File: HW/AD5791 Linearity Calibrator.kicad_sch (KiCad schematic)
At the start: 62 parts, among them J10 Conn_01x01, J11 ISO OUT, J12 ISO OUT, J2 PWR, J3 REF, J4 REF, J5 REF, J6 REF, J7 Conn_01x01, J8 Conn_01x01, J9 Conn_01x01, SW1 RST, U1 Pico, U11 7533, U12 ADuM1201AR, U2 AD5791BRUZ, U3 LM399, U5 ADA4522-1, U6 ADA4522-1, U7 ADA4522-2, U8 78L15, U9 79L15

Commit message: updated files
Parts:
- U3: value LM399 -> ADR1399
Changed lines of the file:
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@@
   (symbol (lib_id "Reference_Voltage:LM399") (at 39.37 60.96 0) (unit 1)
     (in_bom yes) (on_board yes) (dnp no) (fields_autoplaced)
-    (property "Reference" "U3" (at 44.45 60.198 0)
+    (property "Reference" "U3" (at 44.45 59.563 0)
       (effects (font (size 1.27 1.27)) (justify left))
     )
-    (property "Value" "LM399" (at 44.45 62.738 0)
+    (property "Value" "ADR1399" (at 44.45 62.103 0)
       (effects (font (size 1.27 1.27)) (justify left))
     )

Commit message: rearranged files
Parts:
- removed C15, C17, C18, C9: 10uF, Resistor_SMD:R_0603_1608Metric, symbol Device:C_Small
- removed C5, C6, C7: 100uF, Capacitor_SMD:CP_Elec_6.3x5.4, symbol Device:C_Polarized_Small
- removed C8: 10nF, Resistor_SMD:R_0603_1608Metric, symbol Device:C_Small
- removed D1, D2, D4: 5819, Resistor_SMD:R_0603_1608Metric_Pad0.98x0.95mm_HandSolder, symbol Device:D_Small
- removed H1, H2, H3, H5: MountingHole_Pad, MountingHole:MountingHole_3.2mm_M3_Pad_Via, symbol Mechanical:MountingHole_Pad
- removed J10, J7, J8, J9: Conn_01x01, Connector_PinHeader_2.54mm:PinHeader_1x01_P2.54mm_Vertical, symbol Connector_Generic:Conn_01x01
- removed J11, J12: ISO OUT, Connector_PinHeader_2.54mm:PinHeader_1x04_P2.54mm_Vertical, symbol Connector_Generic:Conn_01x04
- removed J2: PWR, Connector_PinHeader_2.54mm:PinHeader_1x03_P2.54mm_Vertical, symbol Connector_Generic:Conn_01x03
- removed J4, J6: REF, Connector_PinHeader_2.54mm:PinHeader_1x02_P2.54mm_Vertical, symbol Connector_Generic:Conn_01x02
- removed JP1: GND BRIDGE, 0603 Jumper:0603 Jumper, symbol Jumper:SolderJumper_2_Open
- removed R1: R, Resistor_SMD:R_0603_1608Metric, symbol Device:R
- removed R10, R12, R13, R9: 10R, Resistor_SMD:R_0603_1608Metric, symbol Device:R
- removed R11: 10K, 0603 Jumper:0603 Jumper, symbol Device:R
- removed R14, R15, R4: 100K, Resistor_SMD:R_0603_1608Metric, symbol Device:R
- removed R2: 1K, Resistor_SMD:R_0603_1608Metric, symbol Device:R
- removed R3: 5R1, Resistor_SMD:R_0603_1608Metric, symbol Device:R
- removed U1: Pico, MCU_RaspberryPi_and_Boards:RPi_Pico_SMD_TH, symbol MCU_RaspberryPi_and_Boards:Pico
- removed U11: 7533, Package_TO_SOT_SMD:SOT-89-3, symbol Regulator_Linear:HT75xx-1-SOT89
- removed U12: ADuM1201AR, Package_SO:SOIC-8_3.9x4.9mm_P1.27mm, symbol Isolator:ADuM1201AR
- removed U5, U6: ADA4522-1, Package_SO:SOIC-8_3.9x4.9mm_P1.27mm, symbol Better Op-Amp:Better_Op-Amp
- removed U8: 78L15, Package_TO_SOT_SMD:SOT-89-3, symbol Regulator_Linear:L78L15_SOT89
- removed U9: 79L15, Package_TO_SOT_SMD:SOT-89-3, symbol Regulator_Linear:L79L15_SOT89
- added C1, C2, C3: 100uF, Capacitor_SMD:CP_Elec_6.3x5.4, symbol Device:C_Polarized_Small
- added C12, C9: 100nF, Capacitor_SMD:C_0603_1608Metric, symbol Device:C_Small
- added C9 (x2): 10uF, Resistor_SMD:R_0603_1608Metric, symbol Device:C_Small
- added J1, J4: ~, 100mm template footprints:CTB93HD3, symbol Connector_Generic:Conn_01x03
- added J11: SIG, Connector_PinHeader_1.27mm:PinHeader_1x04_P1.27mm_Vertical, symbol Connector_Generic:Conn_01x04
- added J11: PWR, Connector_PinHeader_2.54mm:PinHeader_1x04_P2.54mm_Vertical, symbol Connector_Generic:Conn_01x04
- added J2: VREFP, Connector_PinHeader_1.27mm:PinHeader_1x02_P1.27mm_Vertical, symbol Connector_Generic:Conn_01x02
- added J8: VREFN, Connector_PinHeader_1.27mm:PinHeader_1x02_P1.27mm_Vertical, symbol Connector_Generic:Conn_01x02
- added JP1: DACOUT, Connector_PinHeader_1.27mm:PinHeader_1x02_P1.27mm_Vertical, symbol Jumper:SolderJumper_2_Bridged
- added JP2: GND, Connector_PinHeader_1.27mm:PinHeader_1x02_P1.27mm_Vertical, symbol Jumper:SolderJumper_2_Bridged
- added R2: 1K, Resistor_SMD:R_0603_1608Metric, symbol Device:R
- added R2, R3, R4, R5: 10R, Resistor_SMD:R_0603_1608Metric, symbol Device:R
- added R3: 5R1, Resistor_SMD:R_0603_1608Metric, symbol Device:R
- added R4: 100K, Resistor_SMD:R_0603_1608Metric, symbol Device:R
- added U11: L79L15, Package_TO_SOT_SMD:SOT-89-3, symbol Regulator_Linear:L79L15_SOT89
- added U12: 7533, Package_TO_SOT_SMD:SOT-89-3, symbol Regulator_Linear:HT75xx-1-SOT89
- added U13: ADuM1400xRW, Package_SO:SOIC-16W_7.5x10.3mm_P1.27mm, symbol Isolator:ADuM1400xRW
- added U4: L78L15, Package_TO_SOT_SMD:SOT-89-3, symbol Regulator_Linear:L78L15_SOT89
- added U6: REFSCALE, Package_SO:SOIC-8_3.9x4.9mm_P1.27mm, symbol Device:Opamp_Dual
- added U8: Pico, MCU_RaspberryPi_and_Boards:RPi_Pico_SMD_TH, symbol MCU_RaspberryPi_and_Boards:Pico
- added U9: OUTBUF, Package_SO:SOIC-8_3.9x4.9mm_P1.27mm, symbol Device:Opamp_Dual
- C1, C16, C2, C3, C4: footprint Resistor_SMD:R_0603_1608Metric -> Capacitor_SMD:C_0603_1608Metric
- C10, C11, C13, C14: value 10uF -> 100nF; footprint Resistor_SMD:R_0603_1608Metric -> Capacitor_SMD:C_0603_1608Metric
- J3: value REF -> VREFN; footprint Connector_PinHeader_2.54mm:PinHeader_1x02_P2.54mm_Vertical -> Connector_PinHeader_1.27mm:PinHeader_1x02_P1.27mm_Vertical
- J5: value REF -> VREFP; footprint Connector_PinHeader_2.54mm:PinHeader_1x02_P2.54mm_Vertical -> Connector_PinHeader_1.27mm:PinHeader_1x02_P1.27mm_Vertical
- U7: value ADA4522-2 -> REFBUF
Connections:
- net FORCE+ is gone; now on net VREFNF: U7.1
- net FORCE- is gone; now on net VREFPF: U7.7
- net REF is gone; now on net 7VREF: U3.1
- net SENSE+ is gone; now on net VREFNS: U7.2 (-)
- net SENSE- is gone; now on net VREFPS: U7.6 (-)
- net ~{CLR} is gone; now on net +3.3V: U2.7 (~{CLR})
- net ~{RESET} is gone; now on net +3.3V: U2.6 (~{RESET})
- net +15V: now also C2.1, J11.4 (Pin_4), R2.1, R3.1, R4.1, R4.1, U12.2 (VIN), U4.1 (OUT); no longer J3.1 (Pin_1), R6.1, R7.1
- net +3.3V: now also C1.1, C9.2, J11.2 (Pin_2), U12.3 (VOUT), U13.16 (VDD2)
- net -15V: now also R6.1, R7.1, C3.2, J11.3 (Pin_3), R5.1, U11.3 (VO); no longer J5.1 (Pin_1)
- net 7VREF: now also J5.1 (Pin_1), R2.2, R3.1, R4.2, U6.5 (+)
- net ALERT: now also U8.21 (GPIO16)
- net GND: now also C2.2, U2.19 (AGND), U3.2, C1.2, C12.1, C2.2, C3.1, C9.1, C9.1, J1.2 (Pin_2), J11.1 (Pin_1), J2.2 (Pin_2), J4.2 (Pin_2), J8.1 (Pin_1), J8.2 (Pin_2), JP2.1 (A), JP2.2 (B), U11.1 (GND), U12.1 (GND), U13.15 (GND2), U13.9 (GND2), U4.2 (GND), U6.3 (+), U9.5 (+); no longer SW1.1 (A)
- net SCLK: now also U13.5 (VIC), U8.7 (GPIO5); no longer U2.13 (SCLK)
- net SDIN: now also U13.4 (VIB), U8.6 (GPIO4); no longer U2.12 (SDIN)
- net VREFNS: no longer RN1.14 (R3.2), RN1.15 (R2.2)
- net VREFPF: no longer D3.2 (A)
- net VREFPS: no longer RN1.10 (R7.2), RN1.9 (R8.2)
- net ~{LDAC}: now also U13.3 (VIA), U8.5 (GPIO3); no longer U2.8 (~{LDAC})
- net ~{SYNC}: now also U13.6 (VID), U8.9 (GPIO6); no longer U2.14 (~{SYNC})
- net at RN1.6 (R6.1): now also RN1.10 (R7.2); no longer RN1.1 (R1.1)
- net at R7.2: now also C14.2, U6.4 (V-); no longer C11.2
- net at RN1.12 (R5.2): now also RN1.11 (R6.2)
- net at RN1.5 (R5.1): now also RN1.4 (R4.1), U6.2 (-)
- net at SW1.2 (B): now also U8.30 (RUN)
- net at U7.8 (V+): now also C9.2, R2.2
- net at U7.4 (V-): now also C12.2, R5.2
- net at C2.1: now also R3.2
- net at RN1.2 (R2.1), RN1.3 (R3.1): now also U6.6 (-); no longer RN1.16 (R1.2)
- net +10.5V: now reaches D3.1 (K)
- net +10.5V: now also RN1.15 (R2.2), U7.5 (+), J2.1 (Pin_1), R2.1
- net at RN1.13 (R4.2): now also RN1.14 (R3.2)
- net at C13.2: now also R6.2, U9.4 (V-)
- net -10.5V: now reaches U7.3 (+)
- net -10.5V: now also J3.1 (Pin_1), RN1.7 (R7.1), U6.1
- net at C10.2: now also R3.2, U9.8 (V+); no longer R6.2
- net DACOUT renamed BUFIN
- net BUFIN: now also JP1.1 (A), JP1.2 (B), U9.3 (+)
- removed net GNDA: C2.2, U2.19 (AGND), U3.2, U7.5 (+)
- net SDO: no longer names the net of U2.11 (SDO)
- new net: J1.3 (Pin_3), U4.3 (IN)
- new net: J1.1 (Pin_1), U11.2 (VI)
- new net: J4.3 (Pin_3), U9.6 (-), U9.7
- new net: C11.2, R4.2, U6.8 (V+)
- new net: D3.2 (A), U6.7
- new net: J4.1 (Pin_1), U9.1, U9.2 (-)
- new net +3.3VP: C9.2, U13.1 (VDD1), U8.36 (3V3)
- new net GNDD: C9.1, SW1.1 (A), U13.2 (GND1), U13.8 (GND1), U8.13 (GND), U8.18 (GND), U8.23 (GND), U8.28 (GND), U8.3 (GND), U8.33 (AGND), U8.38 (GND), U8.42 (GND), U8.8 (GND)
- new net ISO SCLK: J11.3 (Pin_3), U13.12 (VOC), U2.13 (SCLK)
- new net ISO SDIN: J11.2 (Pin_2), U13.13 (VOB), U2.12 (SDIN)
- new net ISO ~{LDAC}: J11.1 (Pin_1), U13.14 (VOA), U2.8 (~{LDAC})
- new net ISO ~{SYNC}: J11.4 (Pin_4), U13.11 (VOD), U2.14 (~{SYNC})
- now unconnected: RN1.8 (R8.1)
- no-connect marks 10 -> 7
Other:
- note added: ">3mA Iz"
- note added: "cope cage 2333-MS544-10S-ND"
- note removed: "On-board 3V3 reg deactivated"
- note removed: "R should be calculated such that the impedance seen on both pins of the output stage op-amp are the same to prevent bias current errors. AD5791 nominal output imepdance is 3.4K, and assuming a 10K/10K divider with a 5K output impedance, R should be 1.6K. Not particularly important with modern op-amps."
- note removed: "SHORTED BY DEFAULT"
- note removed: "Select for 3mA Iz"

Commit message: further finishing touches
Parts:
- added J10, J11, J12, J13, J9: PWR, Connector_PinHeader_2.54mm:PinHeader_1x02_P2.54mm_Vertical, symbol Connector_Generic:Conn_01x02
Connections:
- net +15V: now also J9.1 (Pin_1)
- net +3.3V: now also J11.1 (Pin_1)
- net -15V: now also J10.1 (Pin_1)
- net GND: now also J10.2 (Pin_2), J11.2 (Pin_2), J12.2 (Pin_2), J13.2 (Pin_2), J9.2 (Pin_2)
- net VCC: now reaches J1.3 (Pin_3), U4.3 (IN)
- net VCC: now also J12.1 (Pin_1)
- net VSS: now reaches J1.1 (Pin_1), U11.2 (VI)
- net VSS: now also J13.1 (Pin_1)
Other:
- moved on the sheet: C1, C10, C11, C12, C13, C14, C2, C3, C9, J1, J11, J2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

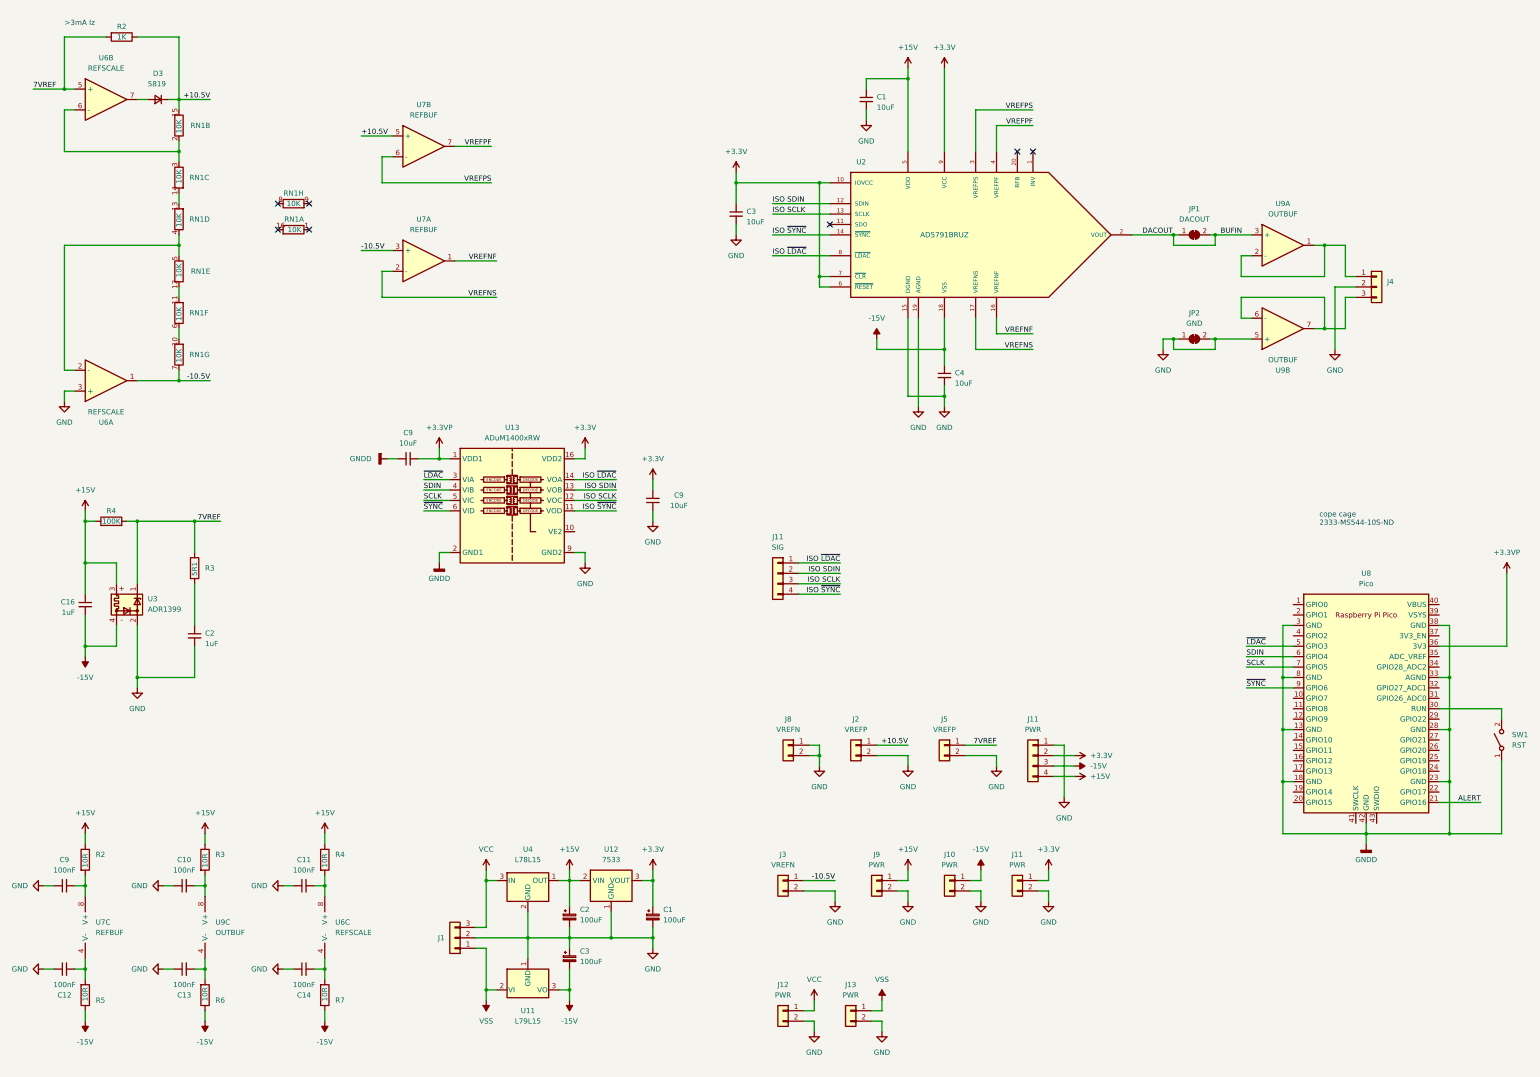
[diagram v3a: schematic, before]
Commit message: Update AD5791 Linearity Calibrator.kicad_sch
added annotations for specific parts choices (op-amps)
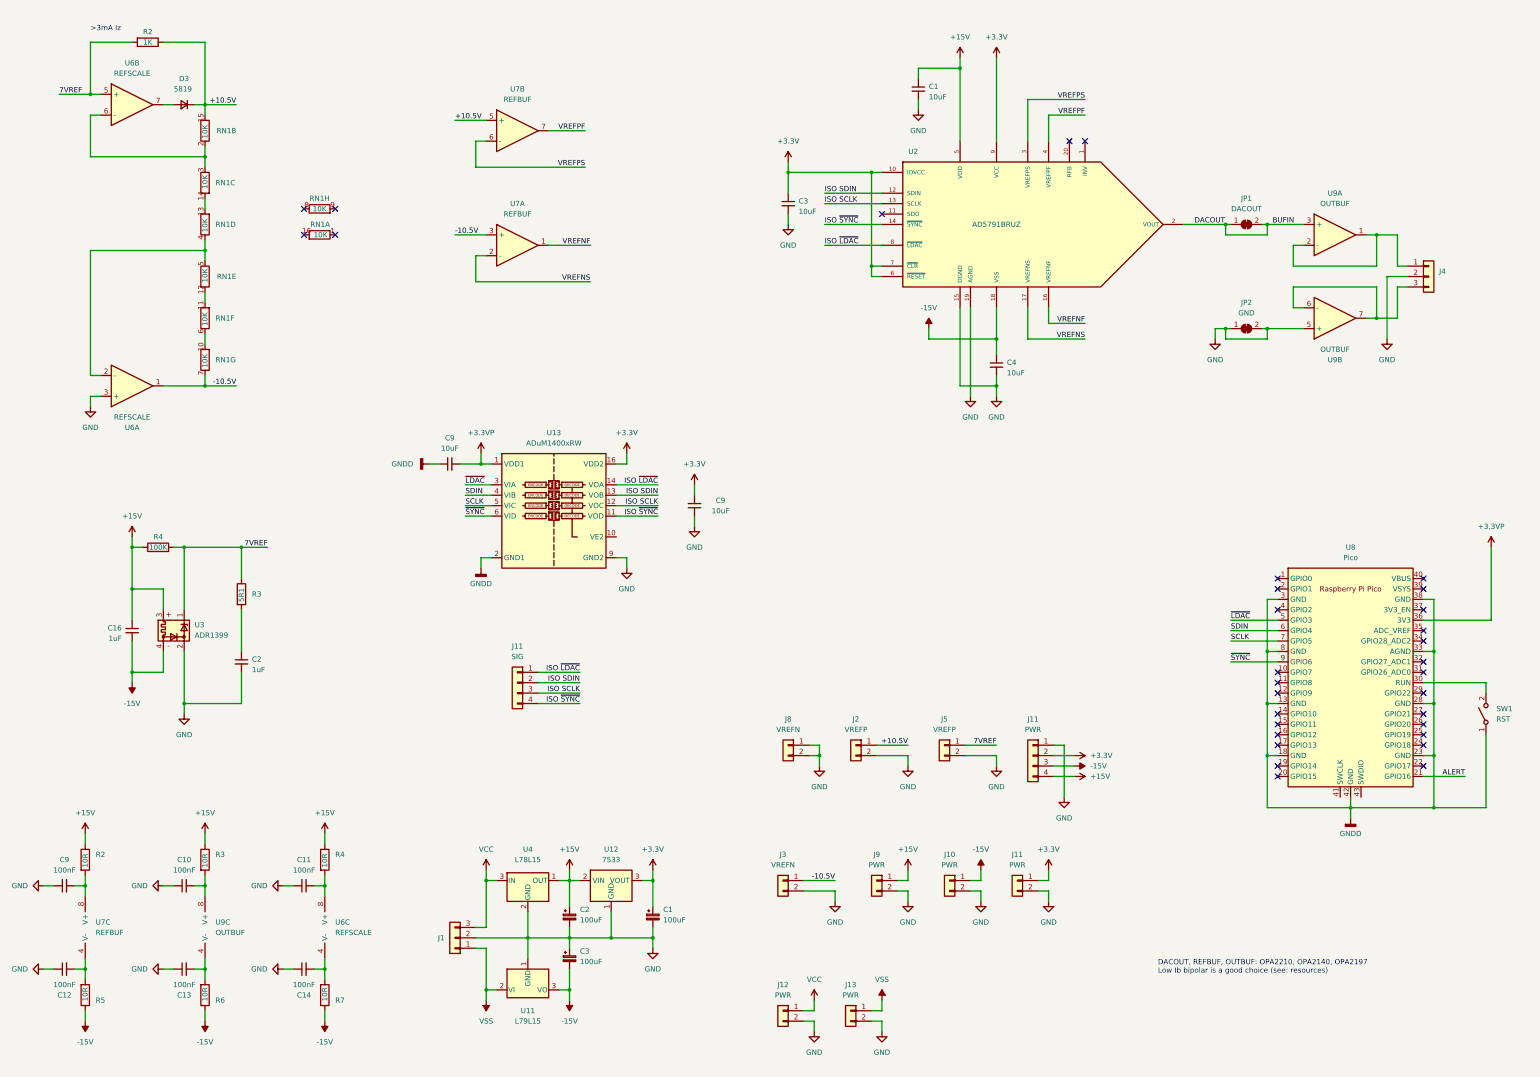
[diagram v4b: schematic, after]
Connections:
- no-connect marks 7 -> 32
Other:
- note added: "DACOUT, REFBUF, OUTBUF: OPA2210, OPA2140, OPA2197 Low Ib bipolar is a good choice (see: resources)"
- note removed: "cope cage 2333-MS544-10S-ND"
- moved on the sheet: C1, C16, C2, C3, C4, C9, D3, J11, J4, JP1, JP2, R2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

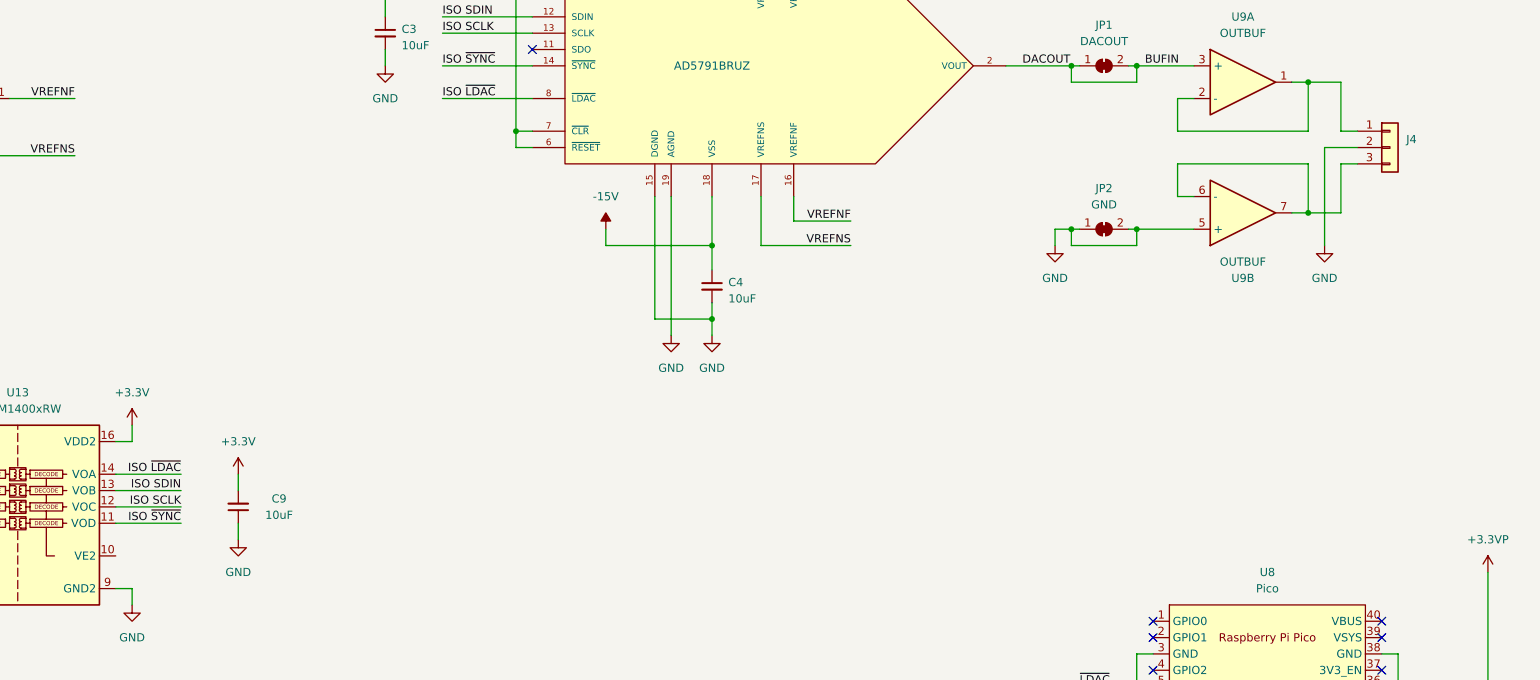
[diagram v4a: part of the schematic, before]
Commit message: added net and silkscreen labels
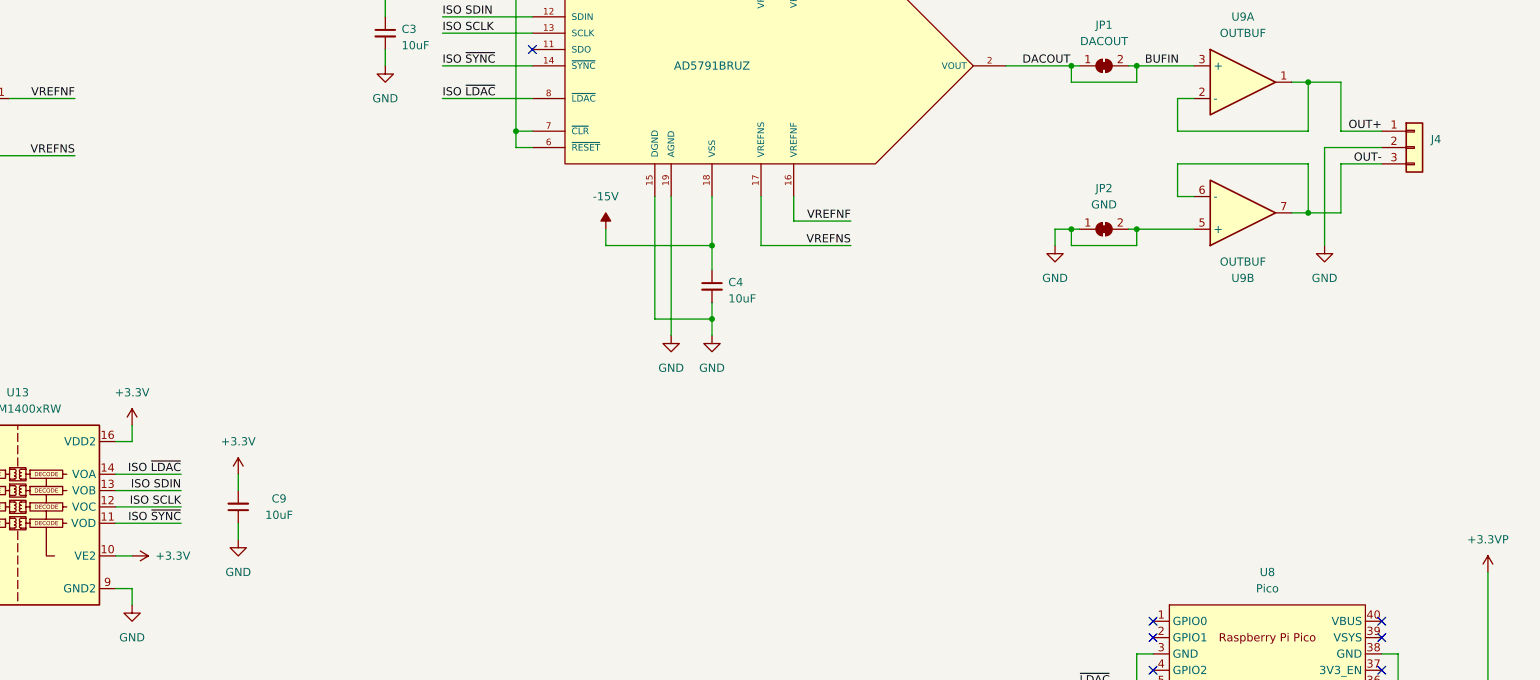
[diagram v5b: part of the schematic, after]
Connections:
- net +3.3V: now also U13.10 (VE2)
- net OUT-: now reaches J4.3 (Pin_3), U9.6 (-), U9.7
- net OUT+: now reaches J4.1 (Pin_1), U9.1, U9.2 (-)
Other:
- moved on the sheet: J4
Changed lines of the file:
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@@
+    (stroke (width 0) (type default))
+  )
+  (wire (pts (xy 171.45 151.13) (xy 168.91 151.13))
     (stroke (width 0) (type default))
   )
@@
     (stroke (width 0) (type default))
   )
-  (wire (pts (xy 356.87 87.63) (xy 361.95 87.63))
+  (wire (pts (xy 356.87 87.63) (xy 365.76 87.63))
     (stroke (width 0) (type default))
   )
@@
     (stroke (width 0) (type default))
   )
-  (wire (pts (xy 359.41 85.09) (xy 361.95 85.09))
+  (wire (pts (xy 359.41 85.09) (xy 365.76 85.09))
     (stroke (width 0) (type default))
   )
@@
     (stroke (width 0) (type default))
   )
-  (wire (pts (xy 361.95 90.17) (xy 359.41 90.17))
+  (wire (pts (xy 365.76 90.17) (xy 359.41 90.17))
     (stroke (width 0) (type default))
   )
@@
     (effects (font (size 1.27 1.27)) (justify left bottom))
   )
+  (label "OUT+" (at 365.76 85.09 180) (fields_autoplaced)
+    (effects (font (size 1.27 1.27)) (justify right bottom))
+  )
   (label "~{SYNC}" (at 132.08 146.05 0) (fields_autoplaced)
     (effects (font (size 1.27 1.27)) (justify left bottom))
@@
   )
   (label "VREFPF" (at 161.29 52.07 180) (fields_autoplaced)
+    (effects (font (size 1.27 1.27)) (justify right bottom))
+  )
+  (label "OUT-" (at 365.76 90.17 180) (fields_autoplaced)
     (effects (font (size 1.27 1.27)) (justify right bottom))
   )
@@
         (path "/e4c8fe5c-4d6c-45a9-911b-05eafd37681e"
           (reference "C13") (unit 1)
+        )
+      )
+    )
+  )
+  (symbol (lib_id "power:+3.3V") (at 171.45 151.13 270) (unit 1)
+    (in_bom yes) (on_board yes) (dnp no)
+    (property "Reference" "#PWR037" (at 167.64 151.13 0)
+      (effects (font (size 1.27 1.27)) hide)
+    )
+    (property "Value" "+3.3V" (at 177.8 151.13 90)
+      (effects (font (size 1.27 1.27)))
+    )
+    (property "Footprint" "" (at 171.45 151.13 0)
+      (effects (font (size 1.27 1.27)) hide)
+    )
+    (property "Datasheet" "" (at 171.45 151.13 0)
+      (effects (font (size 1.27 1.27)) hide)
+    )
+    (pin "1")
+    (instances
+      (project "AD5791 Linearity Calibrator"
+        (path "/545249ea-2c8e-4b30-8f2b-5f4518163292"
+          (reference "#PWR037") (unit 1)
+        )
+      )
+      (project "AD5791 Linearity Calibrator"
+        (path "/e4c8fe5c-4d6c-45a9-911b-05eafd37681e"
+          (reference "#PWR060") (unit 1)
         )
       )
@@
     )
   )
-  (symbol (lib_id "Connector_Generic:Conn_01x03") (at 367.03 87.63 0) (unit 1)
+  (symbol (lib_id "Connector_Generic:Conn_01x03") (at 370.84 87.63 0) (unit 1)
     (in_bom yes) (on_board yes) (dnp no)
-    (property "Reference" "J4" (at 369.57 86.36 0)
-      (effects (font (size 1.27 1.27)) (justify left))
-    )
-    (property "Value" "~" (at 369.57 88.9 0)
-      (effects (font (size 1.27 1.27)) (justify left))
-    )
-    (property "Footprint" "100mm template footprints:CTB93HD3" (at 367.03 87.63 0)
-      (effects (font (size 1.27 1.27)) hide)
-    )
-    (property "Datasheet" "~" (at 367.03 87.63 0)
-      (effects (font (size 1.27 1.27)) hide)
-    )
+    (property "Reference" "J4" (at 373.38 86.36 0)
+      (effects (font (size 1.27 1.27)) (justify left))
+    )
+    (property "Value" "~" (at 373.38 88.9 0)
+      (effects (font (size 1.27 1.27)) (justify left))
+    )
+    (property "Footprint" "100mm template footprints:CTB93HD3" (at 370.84 87.63 0)
+      (effects (font (size 1.27 1.27)) hide)
+    )
+    (property "Datasheet" "~" (at 370.84 87.63 0)
+      (effects (font (size 1.27 1.27)) hide)
+    )

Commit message: minor changes in schem and pcb
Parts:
- J8: value VREFN -> REFCAP
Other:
- moved on the sheet: C16, C2, C9, J10, J11, J2, J3, J5, J8, J9, R3, R4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

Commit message: added linearity chart
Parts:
- renumbered C9 to C15, C9 to C16, C16 to C4, C3 to C5, C1 to C6, C4 to C7, C2 to C8, J11 to J6, J11 to J7, R4 to R1, R2 to R8, R3 to R9, U3 to U10, U2 to U5
